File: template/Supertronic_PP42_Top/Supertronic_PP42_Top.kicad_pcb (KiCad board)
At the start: 2 copper layers, 54 x 65 mm, 4 parts

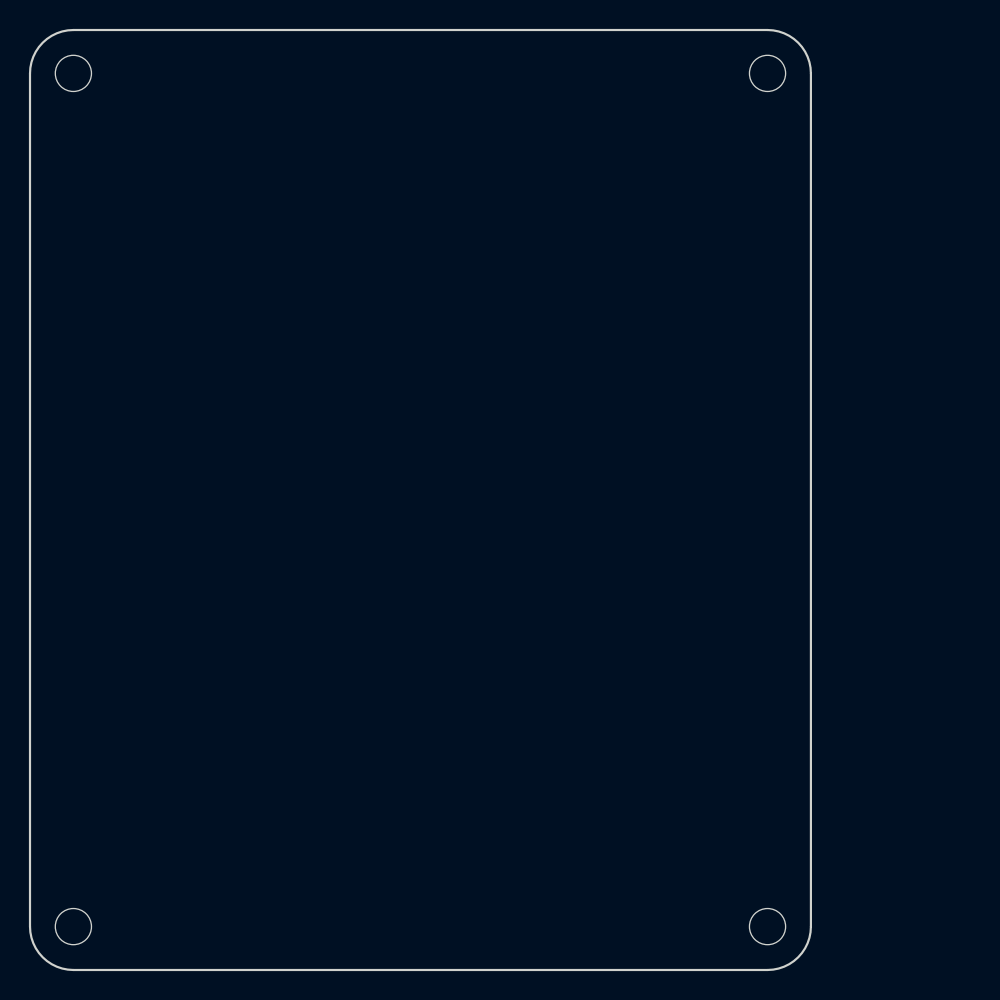
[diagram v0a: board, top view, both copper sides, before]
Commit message: Updated templates
Added mounting holes on schematics, dimensions and re-adjusted board
sizes
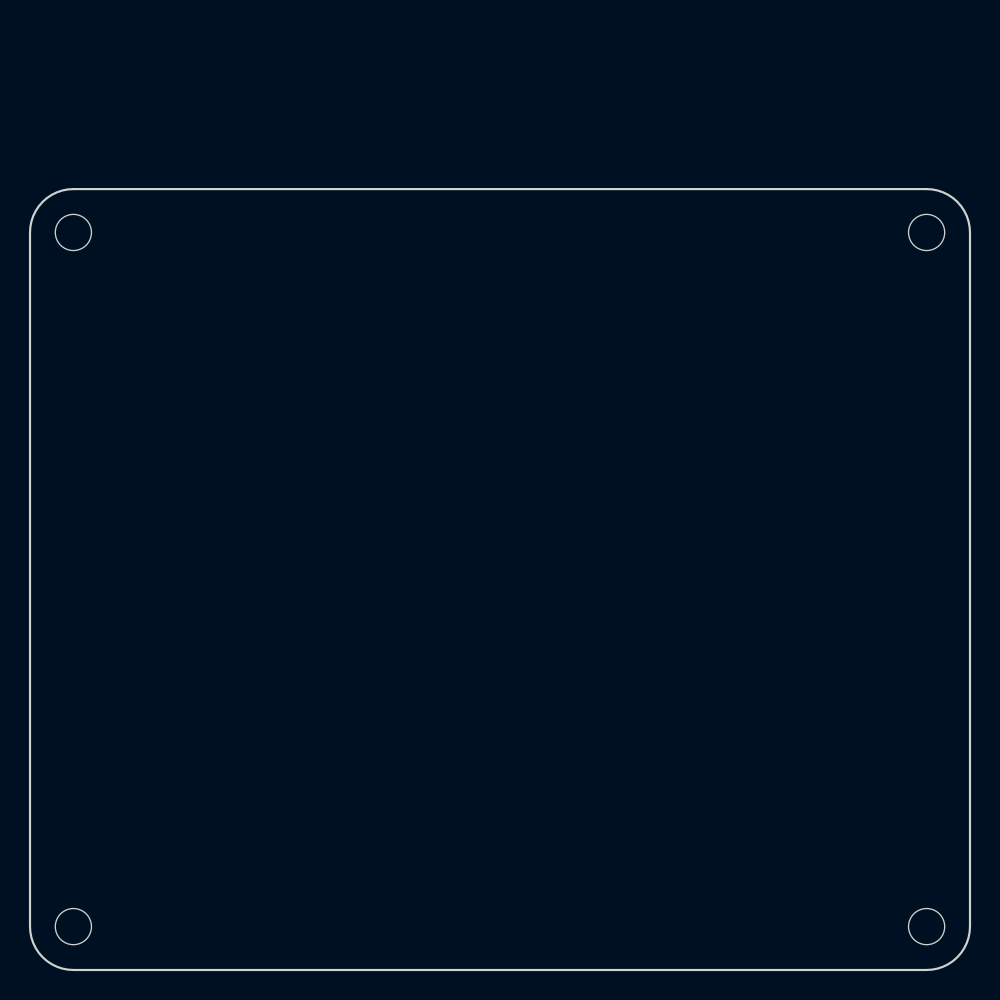
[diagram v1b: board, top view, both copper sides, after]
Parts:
- H1, H2, H3, H4: renamed from REF**; value MountingHole_2.5mm -> MountingHole
- moved H3 59.0 mm to (123.5, 122.5), turned to 90 degrees
- moved H4 59.0 mm to (182.5, 122.5), turned to 90 degrees
- moved H1 49.2 mm to (123.5, 74.5), turned to 90 degrees
- moved H2 49.2 mm to (182.5, 74.5), turned to 90 degrees
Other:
- board size 54 x 65 mm -> 65 x 54 mm
